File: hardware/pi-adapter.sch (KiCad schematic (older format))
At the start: 32 parts, among them P1 CONN_01X04, P10 CONN_01X04, P11 CONN_01X04, P12 CONN_01X04, P13 CONN_01X04, P14 CONN_01X04, P15 CONN_01X04, P16 CONN_01X04, P2 CONN_01X04, P20 CONN_02X20, P21 CONN_01X03, P22 CONN_01X06, P23 CONN_01X03, P3 CONN_01X04, P30 +5V, P31 GND, P4 CONN_01X04, P5 CONN_01X04, P6 CONN_01X04, P7 CONN_01X04, P8 CONN_01X04, P9 CONN_01X04, U1 74HCT245, U2 74HCT245, U3 74HCT245, U4 74HCT245

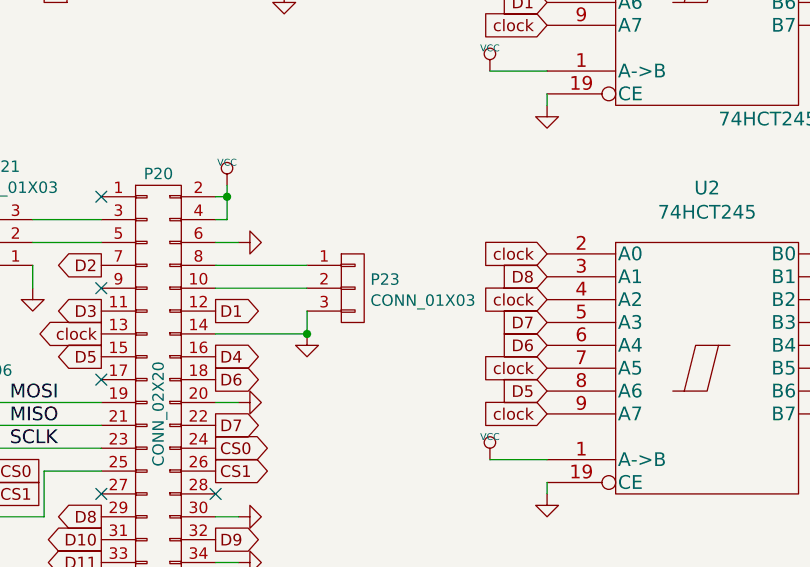
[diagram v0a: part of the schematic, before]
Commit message: o Turn around serial connector to have the gound pin on the (square)   pin 1 on the header.
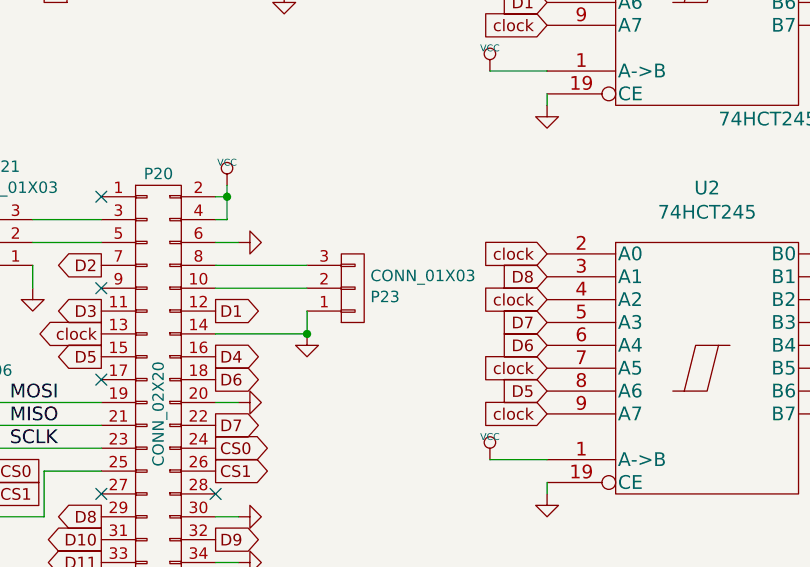
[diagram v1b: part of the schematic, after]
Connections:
- net GND: now also P23.1 (P1); no longer P23.3 (P3)
- net at P20.8 (P8): now also P23.3 (P3); no longer P23.1 (P1)
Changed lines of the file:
@@
 F 3 "" H 3000 3100 50  0000 C CNN
 	1    3000 3100
-	1    0    0    -1
+	1    0    0    1
 $EndComp
 $Comp
